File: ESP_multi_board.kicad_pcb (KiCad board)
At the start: 2 copper layers, 100 x 50 mm, 61 parts, among them IC101 L298, P101 CONN_01X02, P102 CONN_01X06, P103 CONN_01X02, P104 CONN_01X06, P105 CONN_01X06, P106 CONN_01X03, P107 CONN_I2C_MPU6050, P108 CONN_PINES_DIG, P109 CONN_01X04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

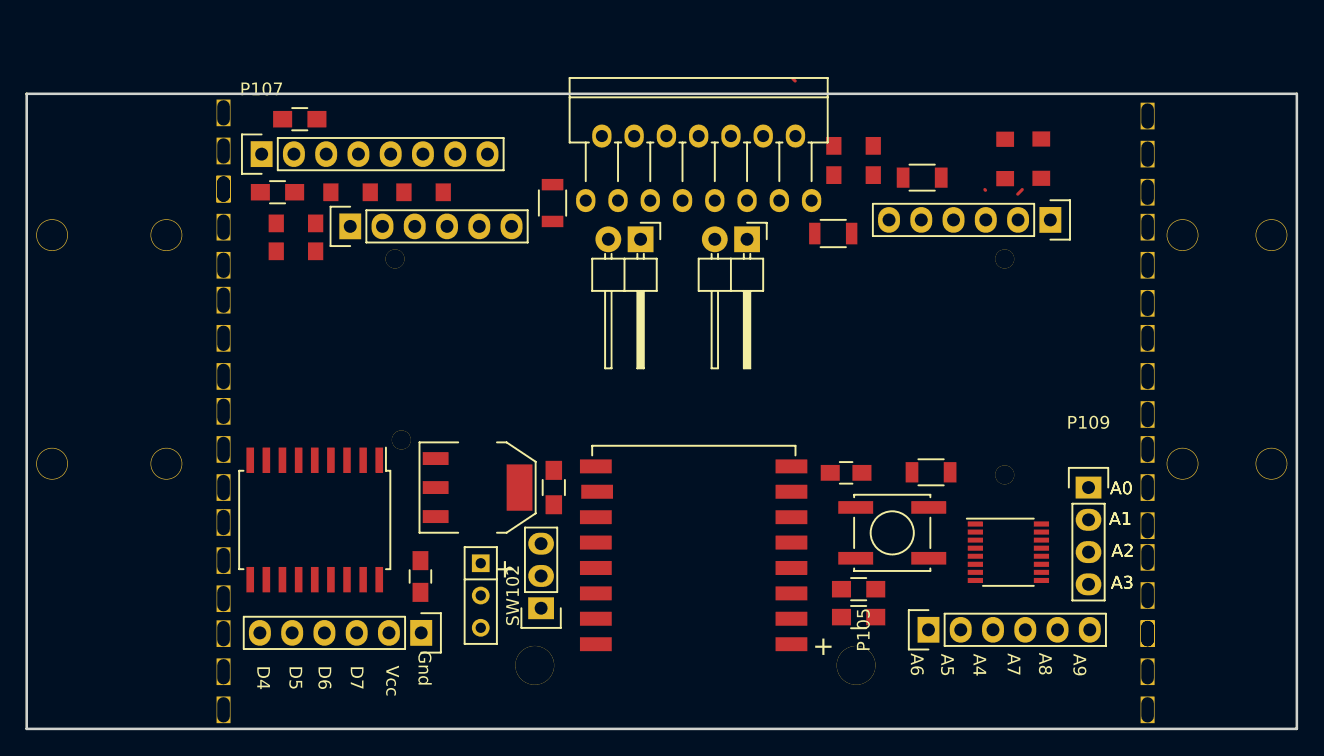
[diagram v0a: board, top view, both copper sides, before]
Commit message: Cambios en el layout y rutado de las pistas de corriente
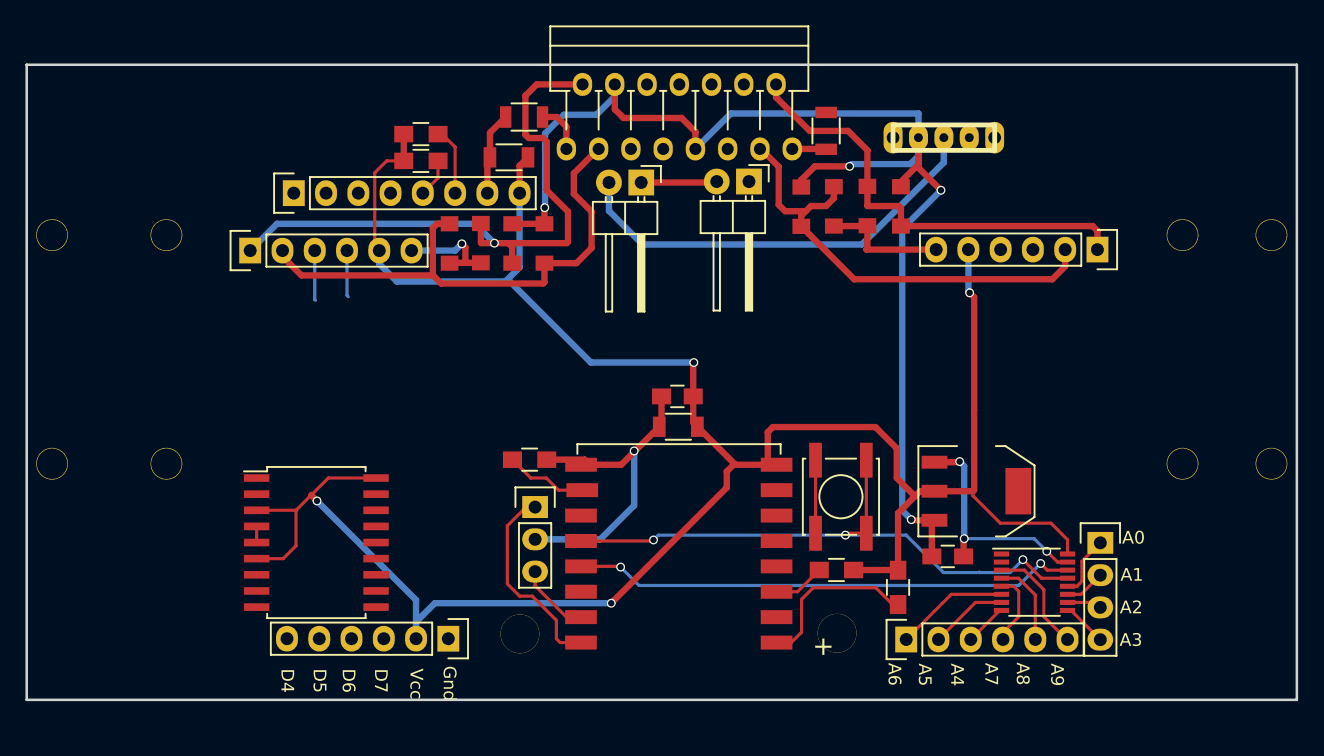
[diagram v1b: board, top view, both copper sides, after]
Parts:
- removed drill5, drill6: 1pin, Connect:1pin
- removed troqel1, troqel2, troquel11, troquel12, troquel13, troquel14, troquel15, troquel16, troquel3, troquel4, troquel5, troquel6: troquel, taladros:troquel_3
- SW102: footprint Buttons_Switches_ThroughHole:SW_Micro_SPST -> switch:switch_power_custom
- moved SW102 51.3 mm to (156.2, 68.5), turned to 0 degrees
- moved C2 41.5 mm to (156.5, 101.4), turned to 0 degrees
- moved U1 39.3 mm to (158.8, 96.3)
- moved C101 32.6 mm to (122.0, 70.0)
- moved C1 20.2 mm to (135.3, 91.2)
- moved D106 19.3 mm to (145.0, 73.9)
- moved D102 17.0 mm to (122.2, 76.8), turned to 270 degrees
- moved C102 14.6 mm to (135.2, 88.8), turned to 0 degrees
- moved D105 12.2 mm to (117.3, 76.8), turned to 270 degrees
- moved R104 12.2 mm to (115.0, 68.2)
- moved D103 11.0 mm to (119.8, 76.8), turned to 270 degrees
- moved D104 10.3 mm to (124.8, 76.8), turned to 270 degrees
- moved R105 10.1 mm to (115.0, 70.3)
- moved D108 9.01 mm to (152.8, 73.9)
- moved P102 8.10 mm to (101.6, 77.3)
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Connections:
- D106 pad 2: M2+ -> M2-
- D107 pad 1: M2+ -> M2-
- D108 pad 2: M2- -> M2+
- D109 pad 1: M2- -> M2+
- IC101 pad 13: M2+ -> M2-
- IC101 pad 14: M2- -> M2+
- P103 pad 1: Net-(P103-Pad1) -> Net-(P101-Pad2)
- P103 pad 2: VCC -> Net-(P103-Pad2)
- SW102 pad 1: Net-(P103-Pad1) -> VCC
- SW102 pad 2: Net-(P101-Pad2) -> Net-(P103-Pad2)
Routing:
- net VDD: track 0.00 -> 189.1 mm, vias 0 -> 4
- net VCC: track 0.00 -> 102.3 mm, vias 0 -> 4
- net GND: track 0.00 -> 76.5 mm, vias 0 -> 5
- net SCL: track 0.00 -> 52.9 mm, vias 0 -> 3
- net M1+: track 0.00 -> 49.3 mm, vias 0 -> 1
- net SDA: track 0.00 -> 42.2 mm, vias 0 -> 2
- net M1-: track 0.00 -> 42.1 mm
- net M2-: track 0.00 -> 36.5 mm
- net M2+: track 0.00 -> 35.5 mm
- net Net-(P103-Pad2): track 0.00 -> 34.3 mm
- net TX: track 0.00 -> 16.6 mm
- net Net-(R102-Pad2): track 0.00 -> 14.1 mm
- net Net-(P105-Pad1): track 0.00 -> 8.97 mm
- net Net-(P105-Pad6): track 0.00 -> 8.71 mm
- net Net-(R103-Pad1): track 0.00 -> 7.09 mm
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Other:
- net class Default: via_dia 0.6 -> 0.7; via_drill 0.4 -> 0.5
- net class power removed

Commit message: Finalizado posible layout
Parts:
- removed drill1, drill12, drill13, drill2: 1pin, Connect:1pin
- added drill8: 1pin, Connect:1pin, F.Cu at (108.7, 89.4)
- added drill8: 1pin, Connect:1pin, F.Cu at (166.8, 89.4)
- moved P104 1.39 mm to (168.4, 75.9)
- moved P102 1.35 mm to (101.8, 76.0)
- moved drill11 1.25 mm to (97.2, 77.2)
- moved drill14 1.25 mm to (97.2, 93.0)
- moved drill3 1.25 mm to (173.8, 93.0)
- moved drill4 1.25 mm to (173.8, 77.2)
- moved R107 0.13 mm to (147.1, 67.9), turned to 270 degrees
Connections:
- U104 pad 10: M1_A -> Net-(P108-Pad3)
- U104 pad 11: M1_B -> Net-(P108-Pad4)
- U104 pad 12: M2_A -> Net-(P108-Pad5)
- U104 pad 13: M2_B -> Net-(P108-Pad6)
- U104 pad 14: Net-(P108-Pad6) -> M2_B
- U104 pad 15: Net-(P108-Pad5) -> M2_A
- U104 pad 16: Net-(P108-Pad4) -> M1_B
- U104 pad 17: Net-(P108-Pad3) -> M1_A
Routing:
- net SCL: track 52.9 -> 147.0 mm, vias 3 -> 6
- net CURRENT1: track 3.95 -> 85.8 mm, vias 0 -> 2
- net SDA: track 42.2 -> 113.8 mm, vias 2 -> 4
- net CURRENT2: track 2.68 -> 68.4 mm, vias 0 -> 2
- net EN2: track 0.00 -> 51.7 mm, vias 0 -> 3
- net M2_B: track 0.00 -> 50.6 mm, vias 0 -> 2
- net M2_A: track 0.00 -> 47.9 mm, vias 0 -> 1
- net ENC2_A: track 0.00 -> 47.7 mm, vias 0 -> 3
- net ENC1_A: track 3.93 -> 50.9 mm, vias 0 -> 1
- net ENC1_B: track 3.67 -> 44.7 mm, vias 0 -> 1
- net EN1: track 0.00 -> 40.7 mm, vias 0 -> 3
- net M1_B: track 0.00 -> 39.7 mm, vias 0 -> 1
- net ENC2_B: track 0.00 -> 39.4 mm, vias 0 -> 3
- net M1_A: track 0.00 -> 37.8 mm
- net GND: track 76.5 -> 95.0 mm, vias 5 -> 10
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- added copper zone on B.Cu, net GND
- added copper zone on F.Cu, net GND
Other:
- board size 100 x 50 mm -> 82.1 x 47.9 mm
- net class Default: trace_width 0.25 -> 0.5
- board text added: "+ -"
- board text added: "3.3V"
- board text added: ">"
- board text added: "GND"
- board text added: "GND 3.3V Enc1B Enc1A M1- M1+"
- board text added: "GND 3.3V Enc2B Enc2A M2- M2+"
- board text added: "GND 3.3V GP0 GP1 GP2 GP3"
- board text added: "OFF|ON"
- board text added: "SCL"
- board text added: "SDA"
- board text added: "TX GND RX"
- board text removed: "D4"
- board text removed: "D5"
- board text removed: "D6"
- board text removed: "D7"
- board text removed: "Gnd"
- board text removed: "Vcc"
